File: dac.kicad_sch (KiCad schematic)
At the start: 27 parts, among them U20 DAC61408RHAR

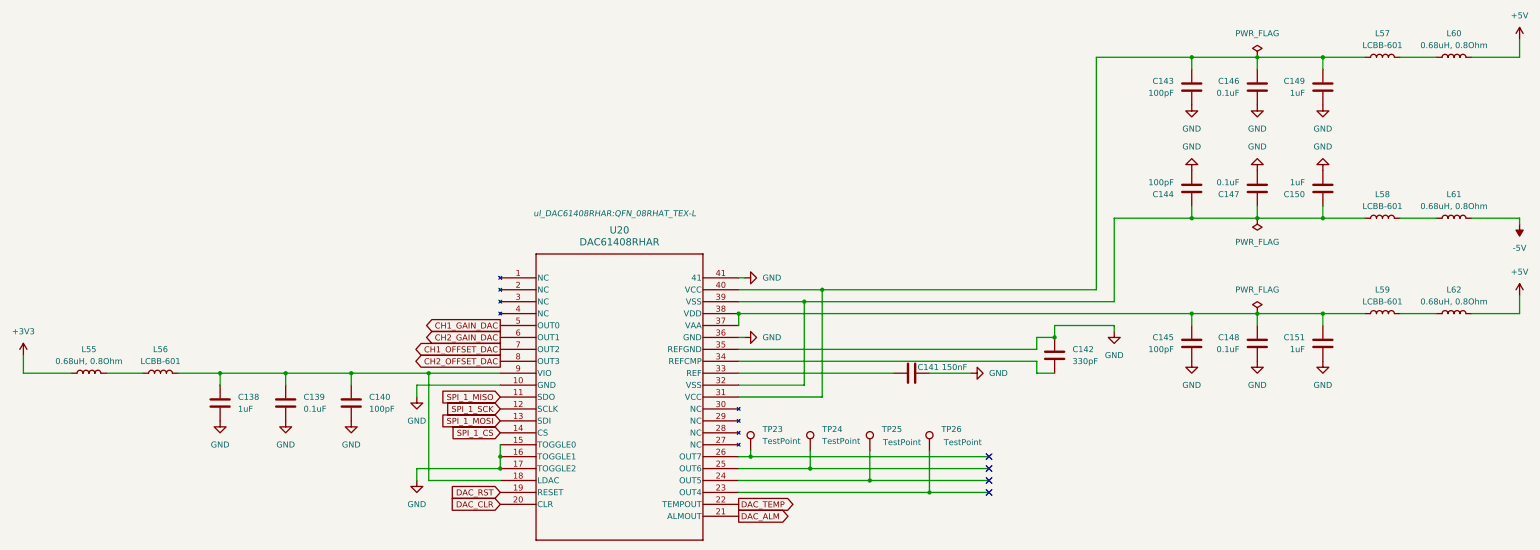
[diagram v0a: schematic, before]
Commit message: Finish channel 1 rework
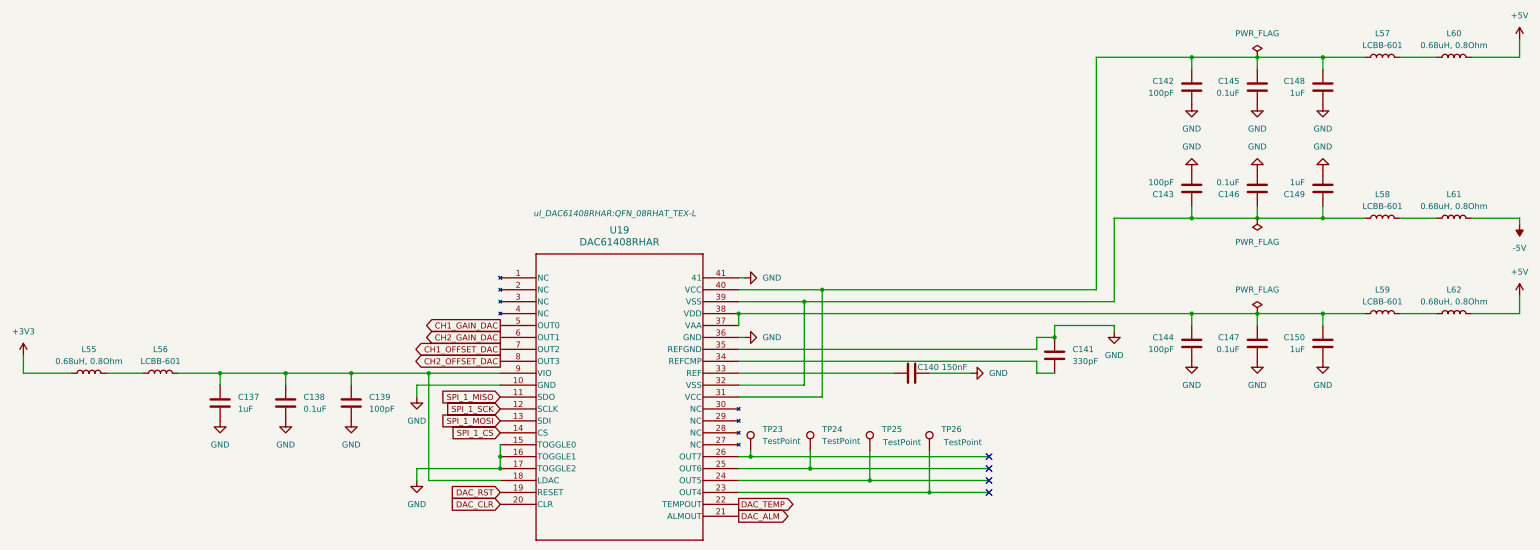
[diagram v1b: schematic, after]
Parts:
- TP23, TP24, TP25, TP26: footprint Connector_PinHeader_2.54mm:PinHeader_1x01_P2.54mm_Vertical -> TestPoint:TestPoint_Pad_D2.0mm
- renumbered C138 to C137, C139 to C138, C140 to C139, C141 to C140, C142 to C141, C143 to C142, C144 to C143, C145 to C144, C146 to C145, C147 to C146, C148 to C147, C149 to C148, C150 to C149, C151 to C150, U20 to U19

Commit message: Place all elements after rework
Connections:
- net TRIGGER_THRESHOLD: now reaches TP26.1, U19.23 (OUT4)
- no-connect marks 4 -> 3
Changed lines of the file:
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@@
-	)
-	(no_connect
-		(at 274.32 171.45)
 	)
 	(no_connect
@@
 			(effects
 				(font
+					(size 1.27 1.27)
+				)
+				(justify left)
+				(hide yes)
+			)
+		)
+	)
+	(global_label "TRIGGER_THRESHOLD"
+		(shape output)
+		(at 274.32 171.45 0)
+		(fields_autoplaced yes)
+		(effects
+			(font
+				(size 1.27 1.27)
+			)
+			(justify left)
+		)
+		(property "Intersheetrefs" "${INTERSHEET_REFS}"
+			(at 296.9599 171.45 0)
+			(effects
+				(font

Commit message: Trying to add symetry
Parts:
- TP23, TP24, TP25, TP26: footprint TestPoint:TestPoint_Pad_D2.0mm -> TestPoint:TestPoint_Pad_D1.0mm
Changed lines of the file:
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@@
 			)
 		)
-		(property "Footprint" "TestPoint:TestPoint_Pad_D2.0mm"
+		(property "Footprint" "TestPoint:TestPoint_Pad_D1.0mm"
 			(at 266.7 162.56 0)
 			(effects
@@
 			)
 		)
-		(property "Footprint" "TestPoint:TestPoint_Pad_D2.0mm"
+		(property "Footprint" "TestPoint:TestPoint_Pad_D1.0mm"
 			(at 228.6 162.56 0)
 			(effects
@@
 			)
 		)
-		(property "Footprint" "TestPoint:TestPoint_Pad_D2.0mm"
+		(property "Footprint" "TestPoint:TestPoint_Pad_D1.0mm"
 			(at 241.3 162.56 0)
 			(effects
@@
 			)
 		)
-		(property "Footprint" "TestPoint:TestPoint_Pad_D2.0mm"
+		(property "Footprint" "TestPoint:TestPoint_Pad_D1.0mm"
 			(at 254 162.56 0)
 			(effects
